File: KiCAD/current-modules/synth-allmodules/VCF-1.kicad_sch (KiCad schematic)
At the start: 58 parts, among them Q12 2N3906, Q13 2N3906, SW17 SW_SPST, U15 TL074, U16 CA3080, U17 CA3080, U18 TL072

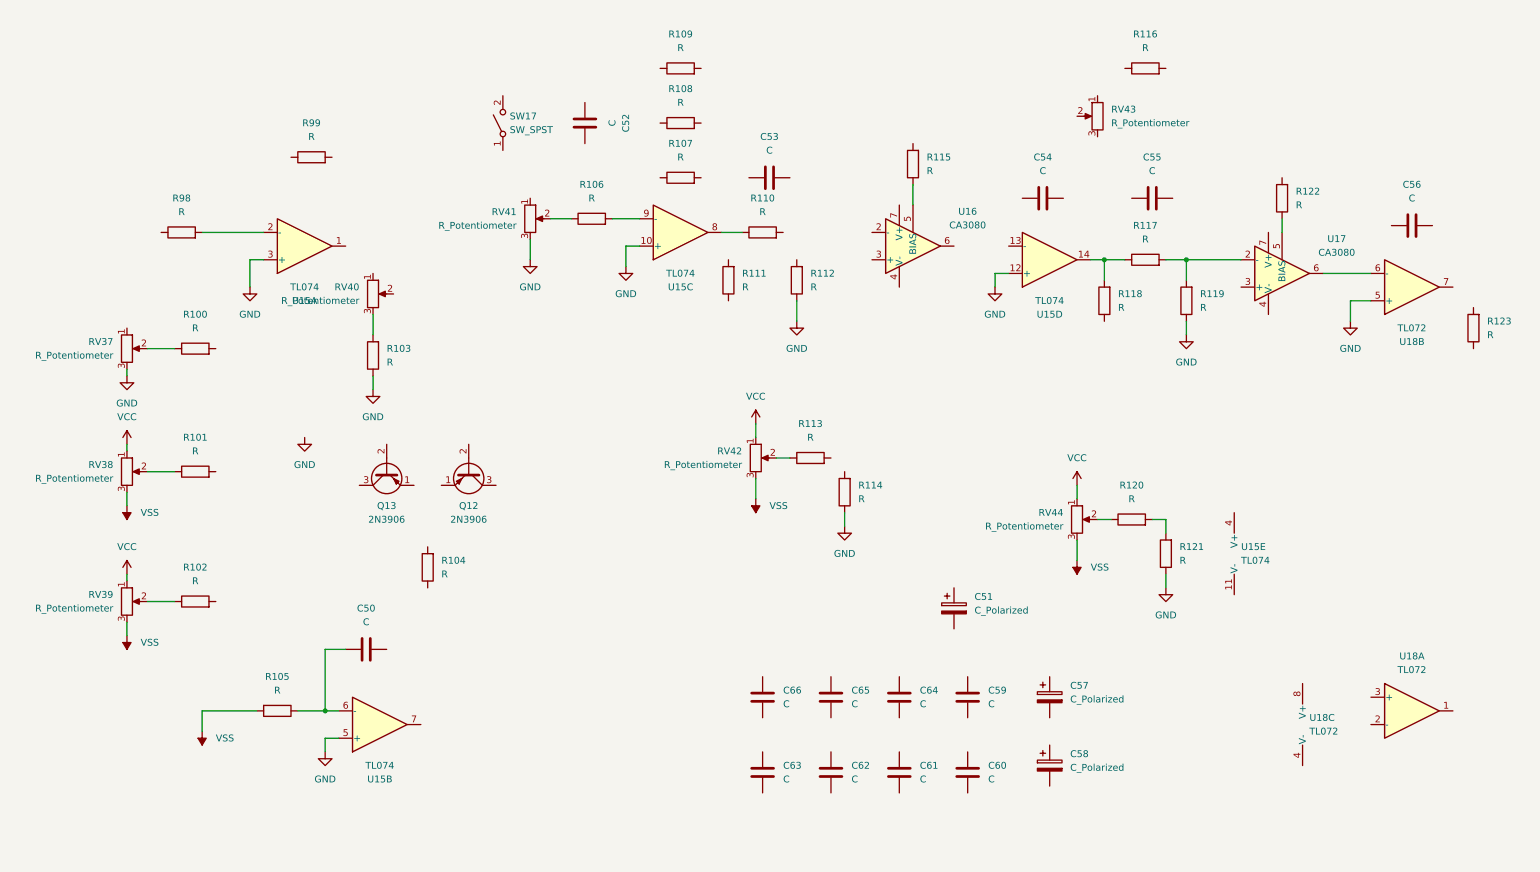
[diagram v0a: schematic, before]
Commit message: VCF-1 Finished (needs jacks)
Additions:
- Component values for VCF-1
- Remaining connections for VCF-1
Changes:
- None
Removals:
- None
NOTES:
- Still needs audio jacks!
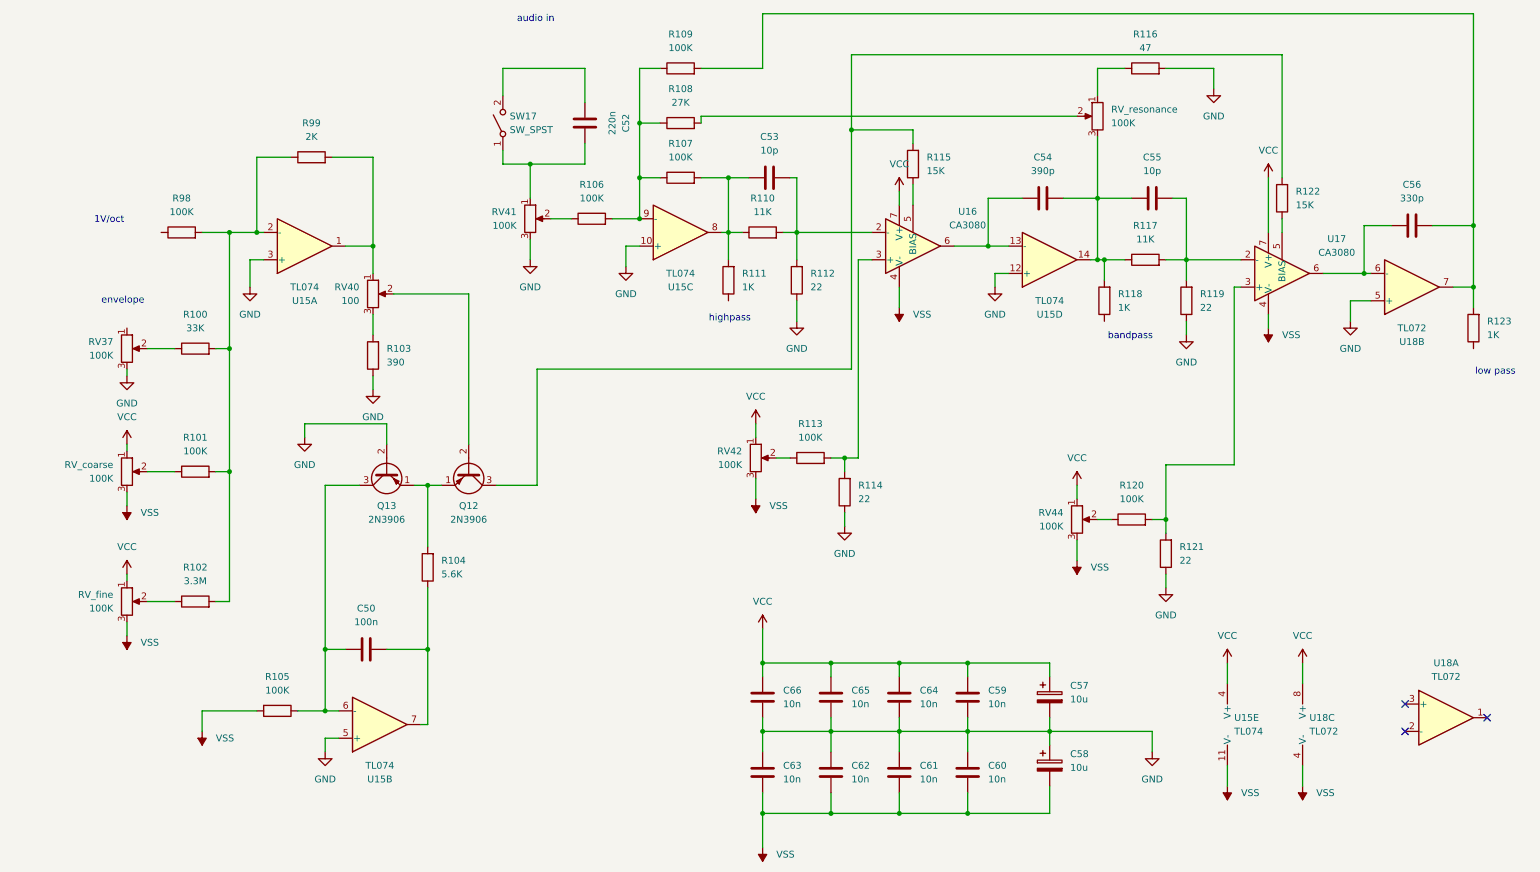
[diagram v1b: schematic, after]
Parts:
- removed C51: C_Polarized, symbol Device:C_Polarized
- C50: value C -> 100n
- C52: value C -> 220n
- C53, C55: value C -> 10p
- C54: value C -> 390p
- C56: value C -> 330p
- C57, C58: value C_Polarized -> 10u
- C59, C60, C61, C62, C63, C64, C65, C66: value C -> 10n
- R100: value R -> 33K
- R101, R105, R106, R107, R109, R113, R120, R98: value R -> 100K
- R102: value R -> 3.3M
- R103: value R -> 390
- R104: value R -> 5.6K
- R108: value R -> 27K
- R110, R117: value R -> 11K
- R111, R118, R123: value R -> 1K
- R112, R114, R119, R121: value R -> 22
- R115, R122: value R -> 15K
- R116: value R -> 47
- R99: value R -> 2K
- RV37, RV41, RV42, RV44: value R_Potentiometer -> 100K
- RV40: value R_Potentiometer -> 100
- RV_coarse: renamed from RV38; value R_Potentiometer -> 100K
- RV_fine: renamed from RV39; value R_Potentiometer -> 100K
- RV_resonance: renamed from RV43; value R_Potentiometer -> 100K
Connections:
- net GND: now also C57.2, C58.1, C59.1, C60.2, C61.2, C62.2, C63.2, C64.1, C65.1, C66.1, Q13.2 (B), R116.2
- net VCC: now also C57.1, C59.2, C64.2, C65.2, C66.2, U15.4 (V+), U16.7 (V+), U17.7 (V+), U18.8 (V+)
- net VSS: now also C58.2, C60.1, C61.1, C62.1, C63.1, U15.11 (V-), U16.4 (V-), U17.4 (V-), U18.4 (V-)
- net at R123.2: now also C56.2, R109.2, U18.7
- net at C55.1: now also C54.2, R117.1, R118.2, RV_resonance.3, U15.14
- net at C55.2: now also R117.2, R119.2, U17.2 (-)
- net at Q13.1 (E): now also Q12.1 (E), R104.2
- net at Q13.3 (C): now also C50.1, R105.1, U15.6 (-)
- net at C53.1: now also R107.2, R110.1, R111.2, U15.8
- net at C53.2: now also R110.2, R112.2, U16.2 (-)
- net at U17.6, U18.6 (-): now also C56.1
- net at U15.13 (-): now also C54.1, U16.6
- net at Q12.2 (B): now also RV40.2
- net at Q12.3 (C): now also R115.2, R122.2
- net at C50.2: now also R104.1, U15.7
- net at R120.2, R121.2: now also U17.3 (+)
- net at R106.2, U15.9 (-): now also R107.1, R108.1, R109.1
- net at R99.1: now also R100.2, R101.2, R102.2, R98.2, U15.2 (-)
- net at R99.2: now also RV40.1, U15.1
- net at R116.1: now also RV_resonance.1
- net at R108.2: now also RV_resonance.2
- net at R113.2: now also R114.2, U16.3 (+)
- net at RV41.1: now also C52.1, SW17.1 (A)
- net at C52.2: now also SW17.2 (B)
- no-connect marks 0 -> 3
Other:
- note added: "1V/oct"
- note added: "audio in"
- note added: "bandpass"
- note added: "envelope"
- note added: "highpass"
- note added: "low pass"
- moved on the sheet: U15E, U18A

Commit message: Audio Jacks
Additions:
- Audio jack IOs for all sheets
Changes:
- None
Removals:
- None
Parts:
- added J28: 1V_OCT, Connector_PinHeader_2.54mm:PinHeader_1x02_P2.54mm_Vertical, symbol Connector_Generic:Conn_01x02
- added J29: ENVELOPE, Connector_PinHeader_2.54mm:PinHeader_1x02_P2.54mm_Vertical, symbol Connector_Generic:Conn_01x02
- added J30: AUDIO_IN, Connector_PinHeader_2.54mm:PinHeader_1x02_P2.54mm_Vertical, symbol Connector_Generic:Conn_01x02
- added J31: HIGHPASS, Connector_PinHeader_2.54mm:PinHeader_1x02_P2.54mm_Vertical, symbol Connector_Generic:Conn_01x02
- added J32: BANDPASS, Connector_PinHeader_2.54mm:PinHeader_1x02_P2.54mm_Vertical, symbol Connector_Generic:Conn_01x02
- added J33: LOWPASS, Connector_PinHeader_2.54mm:PinHeader_1x02_P2.54mm_Vertical, symbol Connector_Generic:Conn_01x02
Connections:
- net GND: now also J28.2 (Pin_2), J29.2 (Pin_2), J30.2 (Pin_2), J31.2 (Pin_2), J32.2 (Pin_2), J33.2 (Pin_2)
- net at R123.1: now also J33.1 (Pin_1)
- net at RV37.1: now also J29.1 (Pin_1)
- net at R98.1: now also J28.1 (Pin_1)
- net at R118.1: now also J32.1 (Pin_1)
- net at R111.1: now also J31.1 (Pin_1)
- net at C52.2, SW17.2 (B): now also J30.1 (Pin_1)
